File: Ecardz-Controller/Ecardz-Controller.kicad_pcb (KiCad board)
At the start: 4 copper layers, 189 x 115 mm, 183 parts, among them IC1 ST25R3916B-AQWT, IC2 INA180A2IDBVR, J1 MEM2061-01-188-00-A, J10 Conn_01x02, J2 Conn_01x04, J3 Conn_01x05, J4 Conn_01x09, J5 Conn_01x01, J6 Conn_01x24, J7 Conn_01x02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

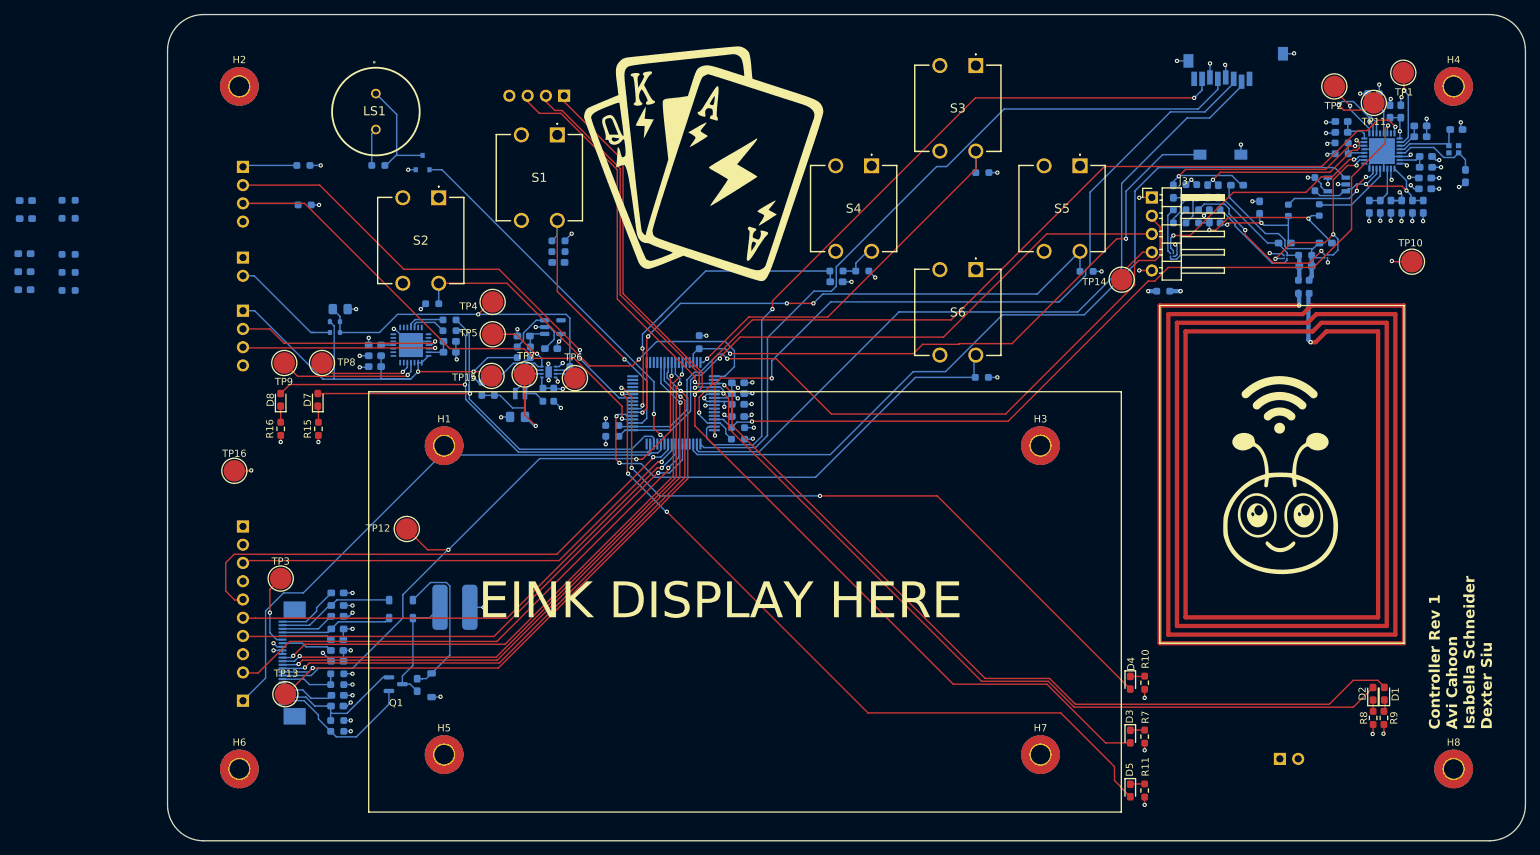
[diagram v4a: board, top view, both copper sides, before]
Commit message: placed button debouncing filter components in layout
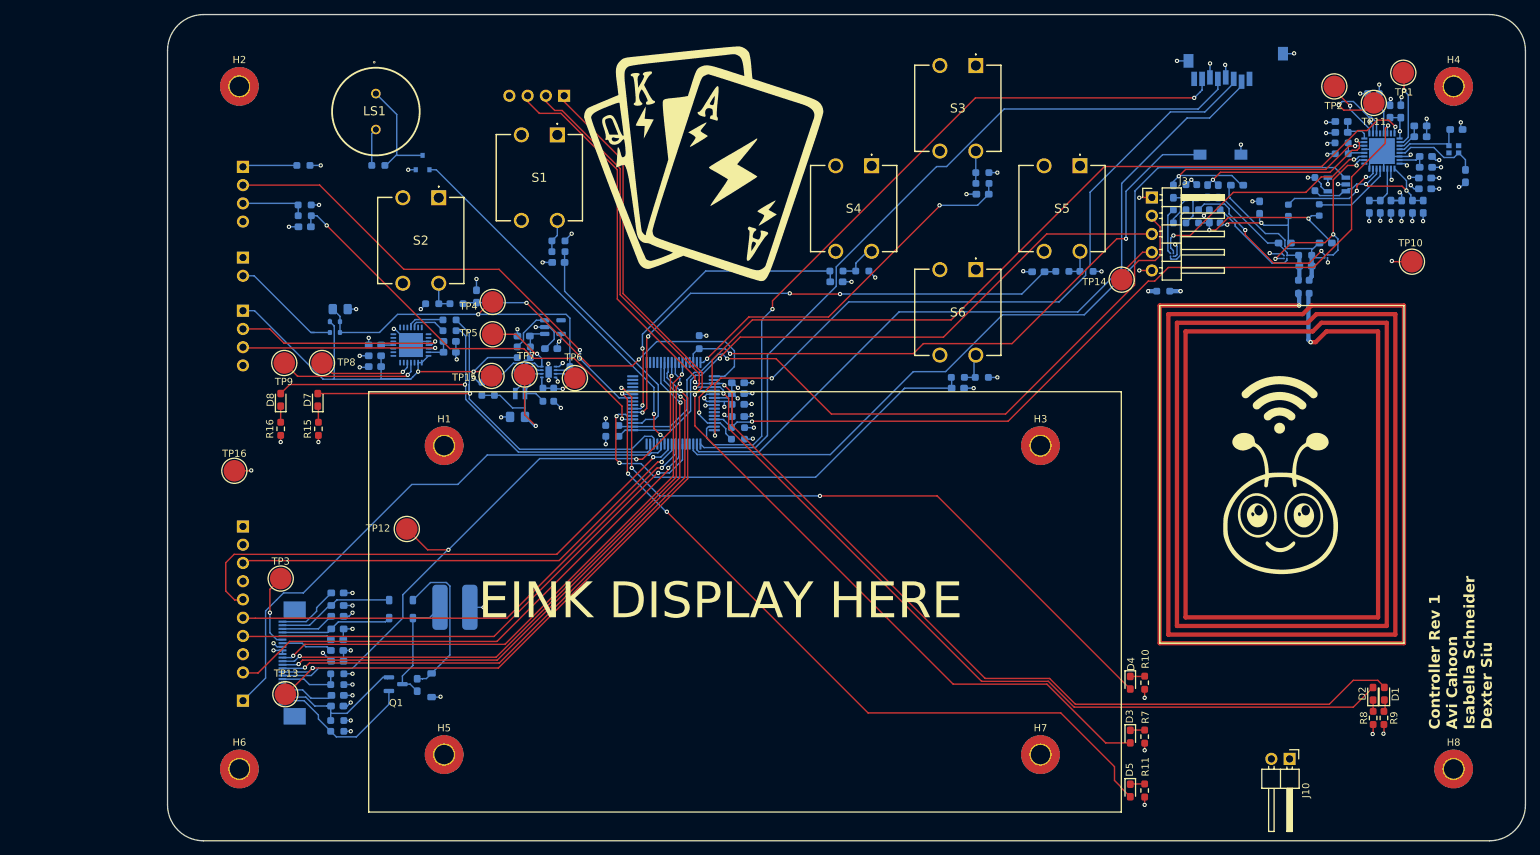
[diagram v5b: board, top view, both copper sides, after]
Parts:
- J10: moved to F.Cu
- moved C58 141.1 mm to (171.2, 125.8)
- moved R55 138.3 mm to (174.5, 125.7), turned to 0 degrees
- moved C56 133.2 mm to (163.4, 115.0)
- moved C59 130.9 mm to (160.0, 142.0), turned to 0 degrees
- moved R53 127.3 mm to (163.4, 113.5)
- moved R56 124.6 mm to (160.0, 140.5), turned to 0 degrees
- moved C55 64.1 mm to (93.0, 129.2), turned to 90 degrees
- moved R52 55.9 mm to (90.2, 130.2)
- moved C60 40.0 mm to (69.1, 119.5)
- moved R57 34.5 mm to (69.1, 118.0)
- moved J10 1.35 mm to (206.2, 193.6)
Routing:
- net /INTERFACE/BUTTON5: track 80.2 -> 4.34 mm, vias 4 -> 0
- net /MCU/BUTTON_5: track 0.00 -> 72.9 mm, vias 0 -> 4
- net /INTERFACE/BUTTON7: track 75.5 -> 9.27 mm, vias 1 -> 0
- net /INTERFACE/BUTTON6: track 68.5 -> 4.72 mm, vias 2 -> 0
- net /MCU/BUTTON_6: track 0.00 -> 62.9 mm, vias 0 -> 2
- net /MCU/BUTTON_7: track 0.00 -> 59.1 mm, vias 0 -> 2
- net /INTERFACE/BUTTON2: track 56.3 -> 4.41 mm, vias 1 -> 0
- net /MCU/BUTTON_3: track 0.00 -> 51.4 mm, vias 0 -> 2
- net /INTERFACE/BUTTON3: track 55.0 -> 4.51 mm, vias 1 -> 0
- net /MCU/BUTTON_2: track 0.00 -> 49.0 mm, vias 0 -> 2
- net /INTERFACE/BUTTON1: track 38.1 -> 4.66 mm, vias 1 -> 0
- net /MCU/BUTTON_1: track 0.00 -> 32.2 mm
- net GND: track 129.4 -> 138.4 mm, vias 82 -> 88
- net /MCU/SD_MOSI: track 106.0 -> 104.6 mm
- net /MCU/SD_SCK: track 103.9 -> 102.5 mm
